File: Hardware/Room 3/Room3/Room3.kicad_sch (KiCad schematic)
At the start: 14 parts, among them Q1 BC547, Q2 BC547, Q3 BC547, SW1 SW_Push

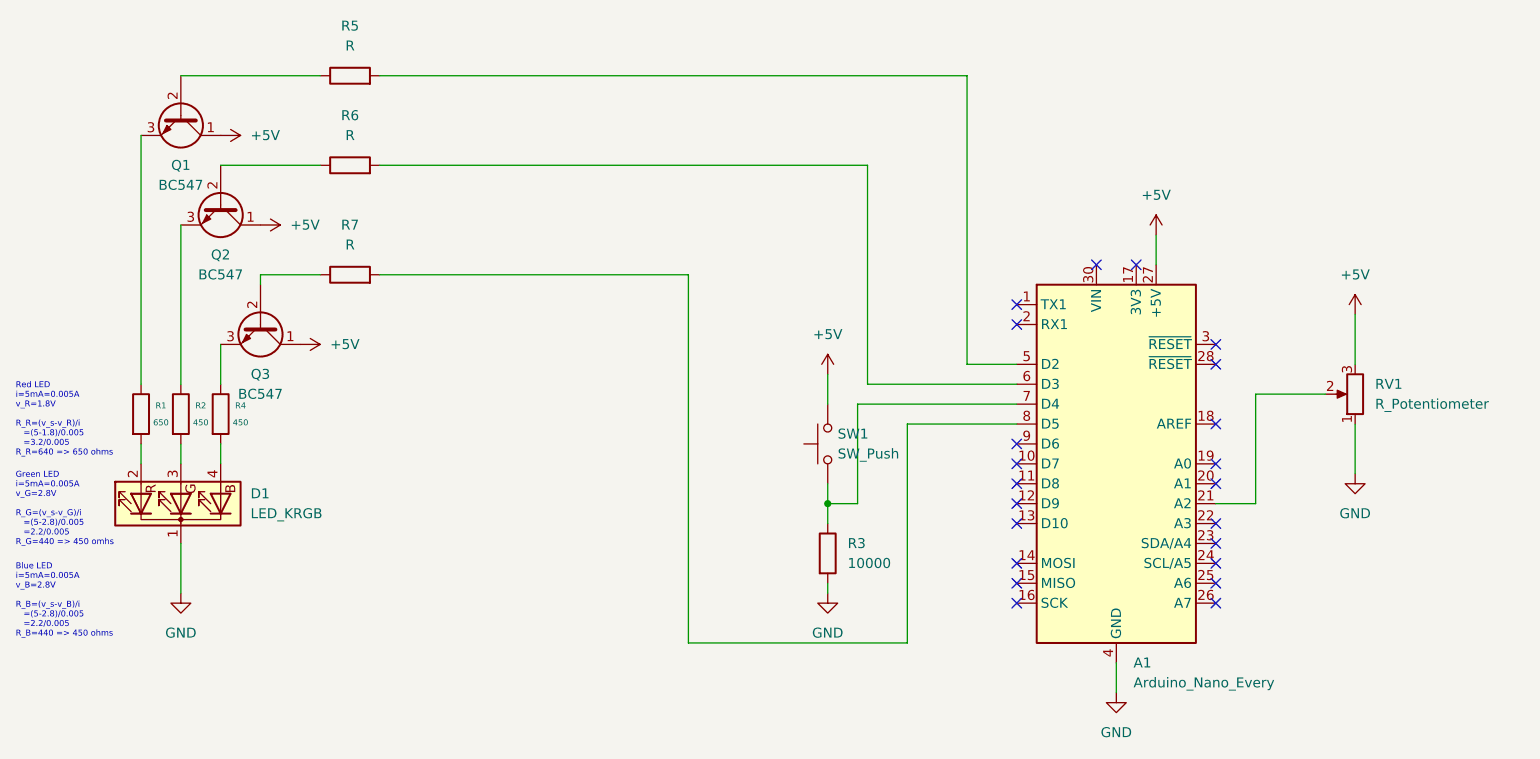
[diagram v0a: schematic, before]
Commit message: Update room 3 schematic
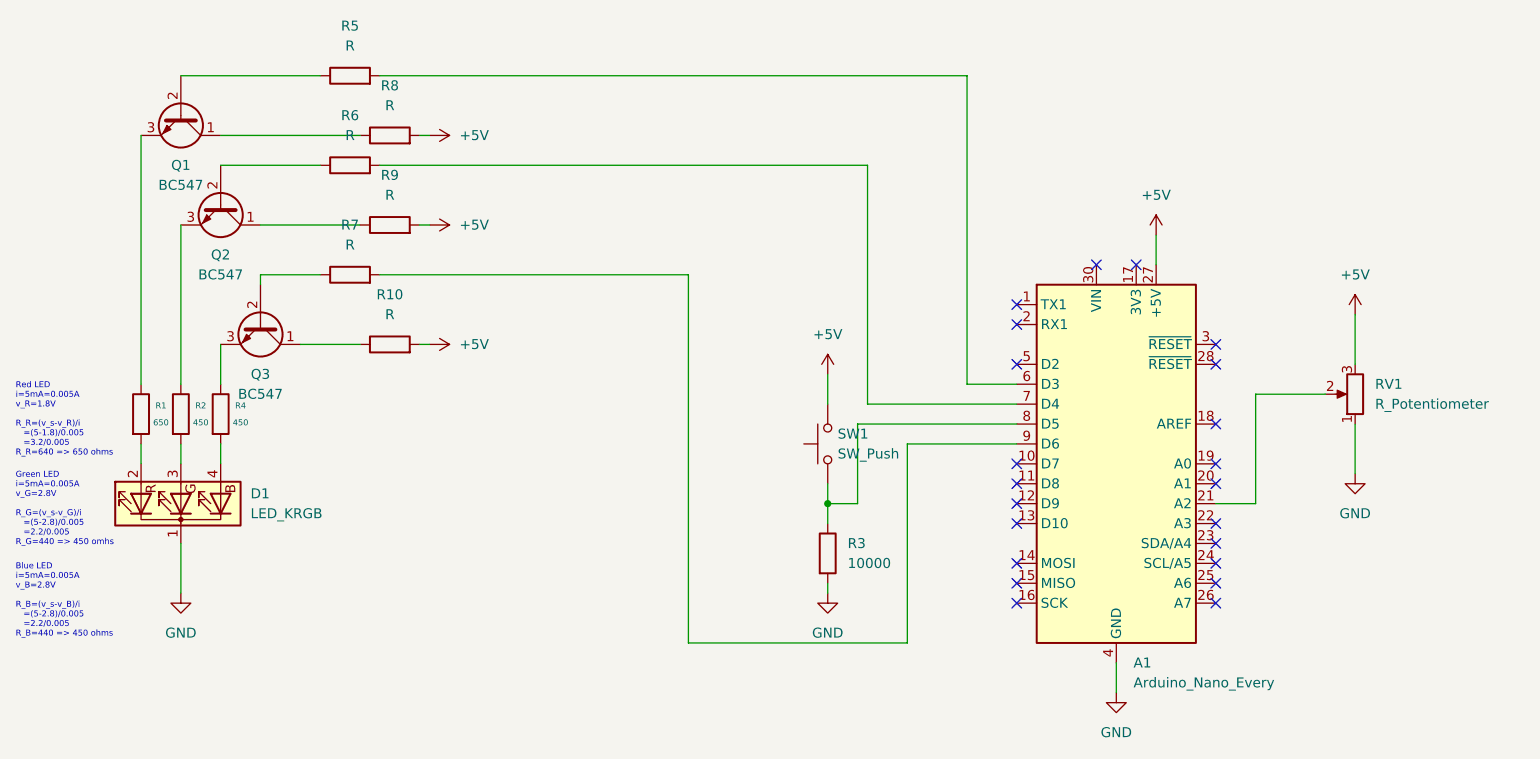
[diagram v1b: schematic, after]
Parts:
- added R10, R8, R9: R, symbol Device:R
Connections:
- net +5V: now also R10.2, R8.2, R9.2; no longer Q1.1 (C), Q2.1 (C), Q3.1 (C)
- net at R5.2: now also A1.6 (D3); no longer A1.5 (D2)
- net at R3.1, SW1.1: now also A1.8 (D5); no longer A1.7 (D4)
- net at R7.2: now also A1.9 (D6); no longer A1.8 (D5)
- net at R6.2: now also A1.7 (D4); no longer A1.6 (D3)
- new net: Q2.1 (C), R9.1
- new net: Q1.1 (C), R8.1
- new net: Q3.1 (C), R10.1

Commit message: Change transistors in room 3 schematic
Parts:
- removed Q1, Q2, Q3: BC547, Package_TO_SOT_THT:TO-92_Inline, symbol Transistor_BJT:BC547
- added Q1, Q2, Q3: BC557, Package_TO_SOT_THT:TO-92_Inline, symbol Transistor_BJT:BC557
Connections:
- net at R5.1: now also Q1.2 (B)
- net at R9.1: now also Q2.3 (E)
- net at R7.1: now also Q3.2 (B)
- net at R4.1: now also Q3.1 (C)
- net at R8.1: now also Q1.3 (E)
- net at R1.1: now also Q1.1 (C)
- net at R10.1: now also Q3.3 (E)
- net at R6.1: now also Q2.2 (B)
- net at R2.1: now also Q2.1 (C)
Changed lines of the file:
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@@
+	)
+	(symbol
+		(lib_id "Transistor_BJT:BC557")
+		(at 34.29 55.88 90)
+		(mirror x)
+		(unit 1)
+		(exclude_from_sim no)
+		(in_bom yes)
+		(on_board yes)
+		(dnp no)
+		(property "Reference" "Q1"
+			(at 33.0199 60.96 0)
+			(effects
+				(font
+					(size 1.27 1.27)
+				)
+				(justify left)
+			)
+		)
+		(property "Value" "BC557"
+			(at 35.5599 60.96 0)
+			(effects
+				(font
+					(size 1.27 1.27)
+				)
+				(justify left)
+			)
+		)
+		(property "Footprint" "Package_TO_SOT_THT:TO-92_Inline"
+			(at 36.195 60.96 0)
+			(effects
+				(font
+					(size 1.27 1.27)
+					(italic yes)
+				)
+				(justify left)
+				(hide yes)
+			)
+		)
+		(property "Datasheet" "https://www.onsemi.com/pub/Collateral/BC556BTA-D.pdf"
+			(at 34.29 55.88 0)
+			(effects
+				(font
+					(size 1.27 1.27)
+				)
+				(justify left)
+				(hide yes)
+			)
+		)
+		(property "Description" "0.1A Ic, 45V Vce, PNP Small Signal Transistor, TO-92"
+			(at 34.29 55.88 0)
+			(effects
+				(font
+					(size 1.27 1.27)
+				)
+				(hide yes)
+			)
+		)
+		(pin "1"
+		)
+		(pin "2"
+		)
+		(pin "3"
+		)
+		(instances
+			(project ""
+				(path "/5f9a8620-ee1b-4e13-ab40-480da1a30c55"
+					(reference "Q1")
+					(unit 1)
+				)
+			)
+		)
 	)
 	(symbol
@@
 	)
 	(symbol
+		(lib_id "Transistor_BJT:BC557")
+		(at 44.45 82.55 90)
+		(mirror x)
+		(unit 1)
+		(exclude_from_sim no)
+		(in_bom yes)
+		(on_board yes)
+		(dnp no)
+		(property "Reference" "Q3"
+			(at 43.1799 87.63 0)
+			(effects
+				(font
+					(size 1.27 1.27)
+				)
+				(justify left)
+			)
+		)
+		(property "Value" "BC557"
+			(at 45.7199 87.63 0)
+			(effects
+				(font
+					(size 1.27 1.27)
+				)
+				(justify left)
+			)
+		)
+		(property "Footprint" "Package_TO_SOT_THT:TO-92_Inline"
+			(at 46.355 87.63 0)
+			(effects
+				(font
+					(size 1.27 1.27)
+					(italic yes)
+				)
+				(justify left)
+				(hide yes)
+			)
+		)
+		(property "Datasheet" "https://www.onsemi.com/pub/Collateral/BC556BTA-D.pdf"
+			(at 44.45 82.55 0)
+			(effects
+				(font
+					(size 1.27 1.27)
+				)
+				(justify left)
+				(hide yes)
+			)
+		)
+		(property "Description" "0.1A Ic, 45V Vce, PNP Small Signal Transistor, TO-92"
+			(at 44.45 82.55 0)
+			(effects
+				(font
+					(size 1.27 1.27)
+				)
+				(hide yes)
+			)
+		)
+		(pin "1"
+		)
+		(pin "2"
+		)
+		(pin "3"
+		)
+		(instances
+			(project "Room3"
+				(path "/5f9a8620-ee1b-4e13-ab40-480da1a30c55"
+					(reference "Q3")
+					(unit 1)
+				)
+			)
+		)
+	)
+	(symbol
 		(lib_id "Switch:SW_Push")
 		(at 116.84 97.79 90)
@@
 	)
 	(symbol
-		(lib_id "Transistor_BJT:BC547")
-		(at 34.29 55.88 270)
-		(unit 1)
-		(exclude_from_sim no)
-		(in_bom yes)
-		(on_board yes)
-		(dnp no)
-		(fields_autoplaced yes)
-		(property "Reference" "Q1"
-			(at 34.29 62.23 90)
-			(effects
-				(font
-					(size 1.27 1.27)
-				)
-			)
-		)
-		(property "Value" "BC547"
-			(at 34.29 64.77 90)
-			(effects
-				(font
-					(size 1.27 1.27)
-				)
-			)
-		)
-		(property "Footprint" "Package_TO_SOT_THT:TO-92_Inline"
-			(at 32.385 60.96 0)
-			(effects
-				(font
-					(size 1.27 1.27)
-					(italic yes)
-				)
-				(justify left)
-				(hide yes)
-			)
-		)
-		(property "Datasheet" "https://www.onsemi.com/pub/Collateral/BC550-D.pdf"
-			(at 34.29 55.88 0)
-			(effects
-				(font
-					(size 1.27 1.27)
-				)
-				(justify left)
-				(hide yes)
-			)
-		)
-		(property "Description" "0.1A Ic, 45V Vce, Small Signal NPN Transistor, TO-92"
-			(at 34.29 55.88 0)
-			(effects
-				(font
-					(size 1.27 1.27)
-				)
-				(hide yes)
-			)
-		)
-		(pin "2"
-		)
-		(pin "1"
-		)
-		(pin "3"
-		)
-		(instances
-			(project ""
-				(path "/5f9a8620-ee1b-4e13-ab40-480da1a30c55"
-					(reference "Q1")
-					(unit 1)
-				)
-			)
-		)
-	)
-	(symbol
 		(lib_id "Device:R")
 		(at 29.21 93.98 0)
@@
 	)
 	(symbol
-		(lib_id "Transistor_BJT:BC547")
-		(at 44.45 82.55 270)
-		(unit 1)
-		(exclude_from_sim no)
-		(in_bom yes)
-		(on_board yes)
-		(dnp no)
-		(fields_autoplaced yes)
-		(property "Reference" "Q3"
-			(at 44.45 88.9 90)
-			(effects
-				(font
-					(size 1.27 1.27)
-				)
-			)
-		)
-		(property "Value" "BC547"
-			(at 44.45 91.44 90)
-			(effects
-				(font
-					(size 1.27 1.27)
-				)
-			)
-		)
-		(property "Footprint" "Package_TO_SOT_THT:TO-92_Inline"
-			(at 42.545 87.63 0)
-			(effects
-				(font
-					(size 1.27 1.27)
-					(italic yes)
-				)
-				(justify left)
-				(hide yes)
-			)
-		)
-		(property "Datasheet" "https://www.onsemi.com/pub/Collateral/BC550-D.pdf"
-			(at 44.45 82.55 0)
-			(effects
-				(font
-					(size 1.27 1.27)
-				)
-				(justify left)
-				(hide yes)
-			)
-		)
-		(property "Description" "0.1A Ic, 45V Vce, Small Signal NPN Transistor, TO-92"
-			(at 44.45 82.55 0)
-			(effects
-				(font
-					(size 1.27 1.27)
-				)
-				(hide yes)
-			)
-		)
-		(pin "3"
-		)
-		(pin "2"
-		)
-		(pin "1"
-		)
-		(instances
-			(project ""
-				(path "/5f9a8620-ee1b-4e13-ab40-480da1a30c55"
-					(reference "Q3")
-					(unit 1)
-				)
-			)
-		)
-	)
-	(symbol
 		(lib_id "Device:R")
 		(at 55.88 62.23 90)
@@
 	)
 	(symbol
+		(lib_id "Transistor_BJT:BC557")
+		(at 39.37 67.31 90)
+		(mirror x)
+		(unit 1)
+		(exclude_from_sim no)
+		(in_bom yes)
+		(on_board yes)
+		(dnp no)
+		(property "Reference" "Q2"
+			(at 38.0999 72.39 0)
+			(effects
+				(font
+					(size 1.27 1.27)
+				)
+				(justify left)
+			)
+		)
+		(property "Value" "BC557"
+			(at 40.6399 72.39 0)
+			(effects
+				(font
+					(size 1.27 1.27)
+				)
+				(justify left)
+			)
+		)
+		(property "Footprint" "Package_TO_SOT_THT:TO-92_Inline"
+			(at 41.275 72.39 0)
+			(effects
+				(font
+					(size 1.27 1.27)
+					(italic yes)
+				)
+				(justify left)
+				(hide yes)
+			)
+		)
+		(property "Datasheet" "https://www.onsemi.com/pub/Collateral/BC556BTA-D.pdf"
+			(at 39.37 67.31 0)
+			(effects
+				(font
+					(size 1.27 1.27)
+				)
+				(justify left)
+				(hide yes)
+			)
+		)
+		(property "Description" "0.1A Ic, 45V Vce, PNP Small Signal Transistor, TO-92"
+			(at 39.37 67.31 0)
+			(effects
+				(font
+					(size 1.27 1.27)
+				)
+				(hide yes)
+			)
+		)
+		(pin "1"
+		)
+		(pin "2"
+		)
+		(pin "3"
+		)
+		(instances
+			(project "Room3"
+				(path "/5f9a8620-ee1b-4e13-ab40-480da1a30c55"
+					(reference "Q2")
+					(unit 1)
+				)
+			)
+		)
+	)
+	(symbol
 		(lib_id "Device:R")
 		(at 60.96 85.09 90)
@@
 					(unit 1)
 				)
-			)
-		)
-	)
-	(symbol
-		(lib_id "Transistor_BJT:BC547")
-		(at 39.37 67.31 270)
-		(unit 1)
-		(exclude_from_sim no)
-		(in_bom yes)
-		(on_board yes)
-		(dnp no)
-		(fields_autoplaced yes)
-		(property "Reference" "Q2"
-			(at 39.37 73.66 90)
-			(effects
-				(font
-					(size 1.27 1.27)
-				)
-			)
-		)
-		(property "Value" "BC547"
-			(at 39.37 76.2 90)
-			(effects
-				(font
-					(size 1.27 1.27)
-				)
-			)
-		)
-		(property "Footprint" "Package_TO_SOT_THT:TO-92_Inline"
-			(at 37.465 72.39 0)
-			(effects
-				(font
-					(size 1.27 1.27)
-					(italic yes)
-				)
-				(justify left)
-				(hide yes)
-			)
-		)
-		(property "Datasheet" "https://www.onsemi.com/pub/Collateral/BC550-D.pdf"
-			(at 39.37 67.31 0)
-			(effects
-				(font
-					(size 1.27 1.27)
-				)
-				(justify left)
-				(hide yes)
-			)
-		)
-		(property "Description" "0.1A Ic, 45V Vce, Small Signal NPN Transistor, TO-92"
-			(at 39.37 67.31 0)
-			(effects
-				(font
-					(size 1.27 1.27)
-				)
-				(hide yes)
-			)
-		)
-		(pin "3"
-		)
-		(pin "1"
-		)
-		(pin "2"
-		)
-		(instances
-			(project ""
-				(path "/5f9a8620-ee1b-4e13-ab40-480da1a30c55"
-					(reference "Q2")
-					(unit 1)
-				)
